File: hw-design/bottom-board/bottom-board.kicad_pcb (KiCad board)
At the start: 2 copper layers, 172 x 140.5 mm, 256 parts, among them J1 JACK_TRS_6PINS, J2 JACK_TRS_6PINS, J3 JACK_TRS_6PINS, J4 JACK_TRS_6PINS, J5 JACK_TRS_6PINS, J6 RJ45_LEDS, J7 Conn_02x50_Odd_Even, J8 Conn_02x50_Odd_Even, K1 IM06TS, K2 IM06TS, P1 USB_B, P2 USB_A, P3 DIN_5, P4 DIN_5, P5 BARREL_JACK, P6 HMI_POWER, P8 HMI_DATA, P9 SERIAL_DEBUG, Q1 2N7002, Q10 2N7002, Q12 2N7002, Q13 2N7002, Q14 BSS84, Q15 BSS84, Q2 2N7002, Q3 J112, Q4 J112, Q5 J112, Q6 J112, Q7 2N7002, Q8 2N7002, Q9 2N7002, SW1 SW_PUSH, U1 MURATA 5V, U10 RT9701, U11 6N137S, U12 ISL83491, U13 AP2120N-3.3, U2 LD1117S50TR_SOT223, U3 CS4245, U4 AT24CS08-STUM, U6 LM4562, U7 LM4562, U8 LM4562, U9 LM4811

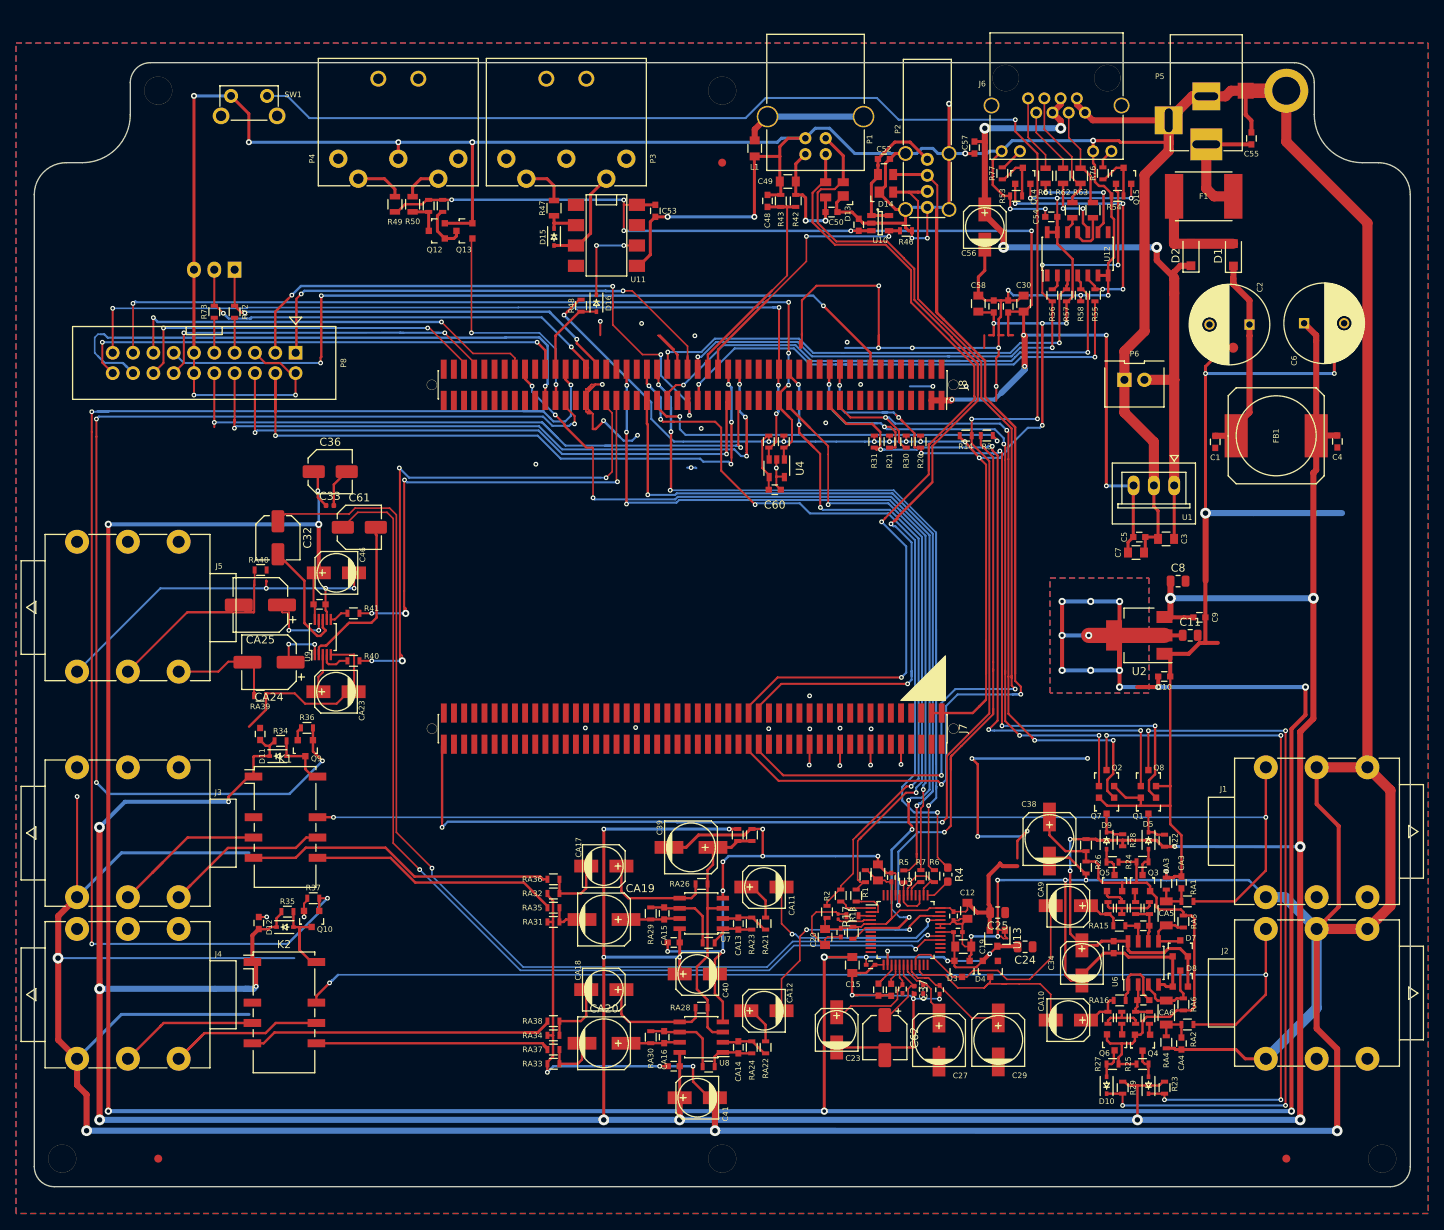
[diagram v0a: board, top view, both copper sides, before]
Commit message: changed a bottomboard to a minimal HMI testing unit
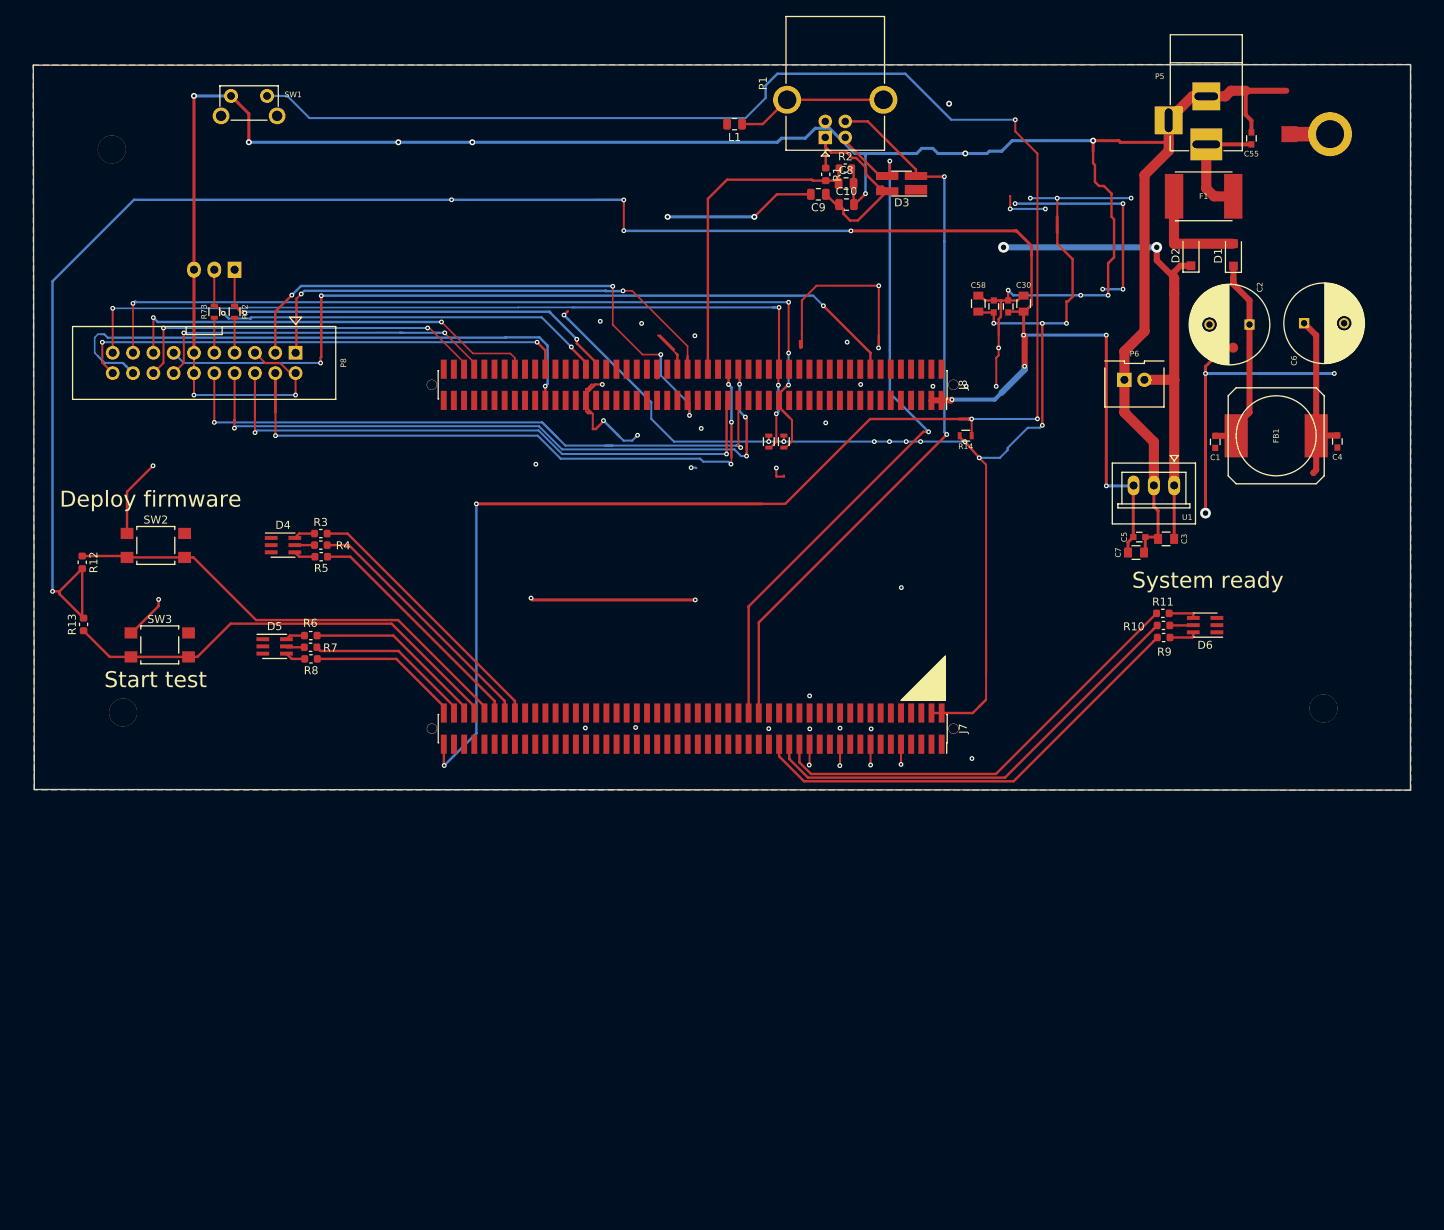
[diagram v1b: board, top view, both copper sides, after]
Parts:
- removed C11, C25: 10uF, Capacitor_SMD:C_0805_2012Metric
- removed C12, C20: 1uF, Capacitors_SMD:C_0805
- removed C13, C14, C16, C17, C21, C22, C26, C28: 100nF, Capacitors_SMD:C_0402
- removed C15, C18, C19, C49: 10uF, Capacitors_SMD:C_0805
- removed C23, C34, C40, C41, C46, C56, CA10, CA11, CA12, CA17, CA18, CA23, CA9: 10uF, Capacitors_SMD:c_elec_5x5.3
- removed C24: 1uF, Capacitor_SMD:C_0805_2012Metric
- removed C27, C29: 47uF, Capacitors_SMD:c_elec_6.3x5.3
- removed C32, C36, C61: 10uF, Capacitor_SMD:C_Elec_5x5.4
- removed C33, C37: 100nF, Capacitor_SMD:C_0402_1005Metric
- removed C35, C42, C43, C44, C45, C47, C48, C50, C51, C52, C53, C54, C57, C60: 100nF, Capacitors_SMD:C_0603
- removed C38, C39: 100uF, Capacitors_SMD:c_elec_6.3x5.3
- removed C62: 10uF, Capacitor_SMD:CP_Elec_5x5.3
- removed CA1, CA2: 2.2nF, Capacitors_SMD:C_0603
- removed CA13, CA14: 33pF, Capacitors_SMD:C_0603
- removed CA15, CA16: 47pF, Capacitors_SMD:C_0603
- removed CA19, CA20: 100uF, Capacitors_SMD:c_elec_6.3x7.7
- removed CA24, CA25: 100uF, Capacitor_SMD:CP_Elec_6.3x7.7
- removed CA3, CA4, CA7, CA8: 100pF, Capacitors_SMD:C_0603
- removed CA5, CA6: 100nF, Capacitors_SMD:C_1206
- removed D10, D11, D12, D15, D16, D9: 1N4148, Diodes_SMD:SOD-323
- removed D13, D14: PRTR5V0U2X, Housings_SOT-23_SOT-143_TSOT-6:SOT-143
- removed D7, D8: BAS70-04, Housings_SOT-23_SOT-143_TSOT-6:SOT-23
- removed FID1, FID2, FID3: FIDUCIAL, footprints:fiducial_in-circuit
- removed H3, H4: HOLE, footprints:Hole_3.5mm
- removed J1, J2, J3, J4, J5: JACK_TRS_6PINS, Connect:NMJ6HCD2
- removed J6: RJ45_LEDS, Connect:RJHSE538X
- removed K1, K2: IM06TS, footprints:Relay_DPDT_Omron_G6S-2F-good_pinout
- removed P2: USB_A, Connect:USB_A_Vertical
- removed P3, P4: DIN_5, Connect:SDS-50J
- removed Q1, Q10, Q12, Q13, Q2, Q7, Q8, Q9: 2N7002, Housings_SOT-23_SOT-143_TSOT-6:SOT-23
- removed Q14, Q15: BSS84, Housings_SOT-23_SOT-143_TSOT-6:SOT-23
- removed Q3, Q4, Q5, Q6: J112, Housings_SOT-23_SOT-143_TSOT-6:SOT-23
- removed R17: 10k, Resistor_SMD:R_0201_0603Metric
- removed R20, R21, R30, R31, R36, R37, R43, R46, R48, R51, R52, R53, R54, R57, R58, RA21, RA22, RA25, RA26, RA27, RA28, RA29, RA30: 10k, Resistors_SMD:R_0603
- removed R22, R23, R28, R29, R34, R35: 100k, Resistors_SMD:R_0603
- removed R24, R25, R26, R27, RA3, RA4, RA5, RA6: 1M, Resistors_SMD:R_0603
- removed R40, R41: 22R, Resistors_SMD:R_0603
- removed R42: 5k6, Resistors_SMD:R_0603
- removed R47, R49, R50: 220R, Resistors_SMD:R_0805
- removed R55, R56, RA15, RA16: 100R, Resistors_SMD:R_0603
- removed R59, R60, R61, R62: 56R, Resistors_SMD:R_0805
- removed R63: 100R, Resistors_SMD:R_0805
- removed R76, R77: 330R, Resistors_SMD:R_0603
- removed RA1, RA2: 47R, Resistors_SMD:R_0603
- removed RA10, RA9: 21k, Resistors_SMD:R_0603
- removed RA11, RA12, RA7, RA8: 1k5, Resistors_SMD:R_0603
- removed RA13, RA14: 4k99, Resistors_SMD:R_0603
- removed RA17, RA18, RA19, RA20: 1k2, Resistors_SMD:R_0603
- removed RA23, RA24: 15k, Resistors_SMD:R_0603
- removed RA31, RA33: 22k, Resistors_SMD:R_0603
- removed RA32, RA34, RA36, RA38: 33R, Resistors_SMD:R_0603
- removed RA35, RA37: 66R, Resistors_SMD:R_0603
- removed RA39, RA40: 75k, Resistors_SMD:R_0603
- removed U10: RT9701, Housings_SOT-23_SOT-143_TSOT-6:SOT-23-5
- removed U11: 6N137S, SMD_Packages:DIP-8_SMD
- removed U12: ISL83491, Housings_SOIC:SOIC-14_3.9x8.7mm_Pitch1.27mm
- removed U13: AP2120N-3.3, Package_TO_SOT_SMD:SOT-23
- removed U2: LD1117S50TR_SOT223, Package_TO_SOT_SMD:SOT-223-3_TabPin2
- removed U3: CS4245, Package_QFP:LQFP-48_7x7mm_P0.5mm
- removed U4: AT24CS08-STUM, Package_TO_SOT_SMD:SOT-23-5
- removed U6, U7, U8: LM4562, Housings_SOIC:SOIC-8_3.9x4.9mm_Pitch1.27mm
- removed U9: LM4811, Housings_SSOP:MSOP-10_3x3mm_Pitch0.5mm
- added R11: 100, Resistor_SMD:R_0603_1608Metric, F.Cu at (201.1, 88.4)
- added R8: 100, Resistor_SMD:R_0603_1608Metric, F.Cu at (94.7, 94.1)
- added SW2: SW_PUSH, Button_Switch_SMD:SW_SPST_TL3305A, F.Cu at (75.3, 79.9)
- added SW3: SW_PUSH, Button_Switch_SMD:SW_SPST_TL3305A, F.Cu at (75.8, 92.3)
- C10: footprint Capacitors_SMD:C_0603 -> Capacitor_SMD:C_0805_2012Metric
- C8: value 10uF -> 100nF
- C9: value 100nF -> 10u; footprint Capacitors_SMD:C_0603 -> Capacitor_SMD:C_0805_2012Metric
- D3: value BAS70-04 -> PRTR5V0U2X; footprint Housings_SOT-23_SOT-143_TSOT-6:SOT-23 -> Package_TO_SOT_SMD:SOT-143_Handsoldering
- D4: value BAS70-04 -> LED_RGB; footprint Housings_SOT-23_SOT-143_TSOT-6:SOT-23 -> LED_SMD:LED_Avago_PLCC6_3x2.8mm
- D5, D6: value 1N4148 -> LED_RGB; footprint Diodes_SMD:SOD-323 -> LED_SMD:LED_Avago_PLCC6_3x2.8mm
- G***: moved to F.Cu
- L1: footprint Capacitors_SMD:C_0805 -> Capacitor_SMD:C_0805_2012Metric
- P1: value USB_B -> USB_B-RESCUE-bottom-board; footprint Connect:USB_B -> Connector_USB:USB_B_OST_USB-B1HSxx_Horizontal
- R1: value 10k -> 5k6; footprint Resistors_SMD:R_0603 -> Resistor_SMD:R_0603_1608Metric
- R10, R3, R5, R6, R7, R9: value 22R -> 100; footprint Resistors_SMD:R_0603 -> Resistor_SMD:R_0603_1608Metric
- R12, R13, R2: value 10k -> 10K; footprint Resistors_SMD:R_0603 -> Resistor_SMD:R_0603_1608Metric
- R4: value 22R -> 100; footprint Resistor_SMD:R_0603_1608Metric_Pad1.05x0.95mm_HandSolder -> Resistor_SMD:R_0603_1608Metric
- moved D5 111.9 mm to (90.1, 92.5), turned to 0 degrees
- moved H2 107.8 mm to (221.2, 100.3)
- moved R12 105.9 mm to (66.1, 82.0), turned to 270 degrees
- moved R13 103.6 mm to (66.2, 89.8), turned to 90 degrees
- moved D4 103.1 mm to (91.2, 79.9), turned to 0 degrees
- moved D3 98.5 mm to (168.5, 34.7)
- moved H1 93.4 mm to (71.2, 100.8)
- moved R2 93.0 mm to (161.5, 32.7), turned to 0 degrees
- moved R4 88.5 mm to (95.9, 79.9), turned to 180 degrees
- moved R1 87.9 mm to (159.0, 33.5), turned to 270 degrees
- moved R3 84.1 mm to (95.9, 78.4), turned to 180 degrees
- moved R6 83.5 mm to (94.6, 91.2), turned to 180 degrees
- moved R5 83.1 mm to (95.9, 81.3), turned to 180 degrees
- moved R7 81.5 mm to (94.6, 92.6), turned to 180 degrees
- moved C9 71.2 mm to (158.1, 36.0), turned to 180 degrees
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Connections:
- C10 pad 1: +5VA -> Net-(C10-Pad1)
- C8 pad 1: +12VA -> USB_DEV_DET
- C9 pad 1: +12VA -> Net-(C10-Pad1)
- D3 pad 2: +5VA -> USB_DEV_DP
- D3 pad 3: CODEC_ADC_A -> USB_DEV_DM
- D4 pad 2: +5VA -> GNDA
- D4 pad 3: CODEC_ADC_B -> GNDA
- D5 pad 1: Net-(D5-Pad1) -> GNDA
- D5 pad 2: Net-(D5-Pad2) -> GNDA
- D6 pad 1: Net-(D6-Pad1) -> GNDA
- D6 pad 2: Net-(D6-Pad2) -> GNDA
- J7 pad 100: Net-(J7-Pad100) -> LED2_R
- J7 pad 11: Net-(J7-Pad11) -> (no net)
- J7 pad 12: Net-(J7-Pad12) -> (no net)
- J7 pad 13: Net-(J7-Pad13) -> (no net)
- J7 pad 14: Net-(J7-Pad14) -> (no net)
- J7 pad 17: Net-(J7-Pad17) -> (no net)
- J7 pad 18: Net-(J7-Pad18) -> (no net)
- J7 pad 19: Net-(J7-Pad19) -> (no net)
- J7 pad 20: Net-(J7-Pad20) -> (no net)
- J7 pad 23: Net-(J7-Pad23) -> (no net)
- J7 pad 24: Net-(J7-Pad24) -> (no net)
- J7 pad 25: Net-(J7-Pad25) -> (no net)
- J7 pad 26: Net-(J7-Pad26) -> (no net)
- J7 pad 29: Net-(J7-Pad29) -> LED3_R
- J7 pad 30: Net-(J7-Pad30) -> (no net)
- J7 pad 31: Net-(J7-Pad31) -> LED3_G
- J7 pad 32: Net-(J7-Pad32) -> (no net)
- J7 pad 33: Net-(J7-Pad33) -> LED3_B
- J7 pad 34: Net-(J7-Pad34) -> (no net)
- J7 pad 37: USB_HOST_DP -> (no net)
- J7 pad 39: USB_HOST_DM -> (no net)
- J7 pad 42: Net-(J7-Pad42) -> (no net)
- J7 pad 43: Net-(J7-Pad43) -> (no net)
- J7 pad 44: Net-(J7-Pad44) -> (no net)
- J7 pad 45: Net-(J7-Pad45) -> (no net)
- J7 pad 46: Net-(J7-Pad46) -> (no net)
- J7 pad 48: Net-(J7-Pad48) -> (no net)
- J7 pad 49: Net-(J7-Pad49) -> (no net)
- J7 pad 5: Net-(J7-Pad5) -> (no net)
- J7 pad 50: Net-(J7-Pad50) -> (no net)
- J7 pad 51: Net-(J7-Pad51) -> (no net)
- J7 pad 52: Net-(J7-Pad52) -> (no net)
- J7 pad 53: Net-(J7-Pad53) -> (no net)
- J7 pad 54: Net-(J7-Pad54) -> (no net)
- J7 pad 55: Net-(J7-Pad55) -> (no net)
- J7 pad 56: Net-(J7-Pad56) -> (no net)
- J7 pad 57: Net-(J7-Pad57) -> (no net)
- J7 pad 58: Net-(J7-Pad58) -> (no net)
- J7 pad 59: Net-(J7-Pad59) -> (no net)
- J7 pad 6: Net-(J7-Pad6) -> (no net)
- J7 pad 60: Net-(J7-Pad60) -> (no net)
- J7 pad 63: Net-(J7-Pad63) -> (no net)
- J7 pad 64: Net-(J7-Pad64) -> (no net)
- J7 pad 65: Net-(J7-Pad65) -> (no net)
- J7 pad 66: Net-(J7-Pad66) -> (no net)
- J7 pad 67: Net-(J7-Pad67) -> (no net)
- J7 pad 68: Net-(J7-Pad68) -> (no net)
- J7 pad 69: Net-(J7-Pad69) -> (no net)
- J7 pad 7: Net-(J7-Pad7) -> (no net)
- J7 pad 70: Net-(J7-Pad70) -> (no net)
- J7 pad 71: Net-(J7-Pad71) -> (no net)
- J7 pad 73: Net-(J7-Pad73) -> (no net)
- J7 pad 74: Net-(J7-Pad74) -> (no net)
- J7 pad 75: Net-(J7-Pad75) -> (no net)
- J7 pad 76: Net-(J7-Pad76) -> (no net)
- J7 pad 77: Net-(J7-Pad77) -> (no net)
- J7 pad 78: Net-(J7-Pad78) -> (no net)
- J7 pad 79: Net-(J7-Pad79) -> (no net)
- J7 pad 8: Net-(J7-Pad8) -> (no net)
- J7 pad 80: Net-(J7-Pad80) -> (no net)
- J7 pad 81: Net-(J7-Pad81) -> (no net)
- J7 pad 82: Net-(J7-Pad82) -> (no net)
- J7 pad 83: Net-(J7-Pad83) -> (no net)
- J7 pad 84: Net-(J7-Pad84) -> (no net)
- J7 pad 85: Net-(J7-Pad85) -> (no net)
- J7 pad 86: Net-(J7-Pad86) -> LED1_B
- J7 pad 87: Net-(J7-Pad87) -> (no net)
- J7 pad 88: Net-(J7-Pad88) -> LED1_G
- J7 pad 89: Net-(J7-Pad89) -> (no net)
- J7 pad 90: Net-(J7-Pad90) -> LED1_R
- J7 pad 91: Net-(J7-Pad91) -> (no net)
- J7 pad 92: Net-(J7-Pad92) -> Button1
- J7 pad 93: Net-(J7-Pad93) -> (no net)
- J7 pad 94: Net-(J7-Pad94) -> Button2
- J7 pad 95: Net-(J7-Pad95) -> (no net)
- J7 pad 96: Net-(J7-Pad96) -> LED2_B
- J7 pad 97: Net-(J7-Pad97) -> (no net)
- J7 pad 98: Net-(J7-Pad98) -> LED2_G
- J8 pad 100: Net-(J8-Pad100) -> (no net)
- J8 pad 11: Net-(J8-Pad11) -> (no net)
- J8 pad 12: Net-(J8-Pad12) -> (no net)
- J8 pad 13: Net-(J8-Pad13) -> (no net)
- J8 pad 14: Net-(J8-Pad14) -> (no net)
- J8 pad 15: Net-(J8-Pad15) -> (no net)
- J8 pad 17: Net-(J8-Pad17) -> (no net)
- J8 pad 19: Net-(J8-Pad19) -> (no net)
- J8 pad 20: Net-(J8-Pad20) -> (no net)
- J8 pad 21: LEFT_GAIN_CTRL2 -> (no net)
- J8 pad 22: LEFT_GAIN_CTRL1 -> (no net)
- J8 pad 23: RIGHT_GAIN_CTRL2 -> (no net)
- J8 pad 24: RIGHT_GAIN_CTRL1 -> (no net)
- J8 pad 25: Net-(J8-Pad25) -> (no net)
- J8 pad 26: Net-(J8-Pad26) -> (no net)
- J8 pad 27: Net-(J8-Pad27) -> (no net)
- J8 pad 28: Net-(J8-Pad28) -> (no net)
- J8 pad 29: Net-(J8-Pad29) -> (no net)
- J8 pad 30: Net-(J8-Pad30) -> (no net)
- J8 pad 31: CODEC_I2C_SCL -> (no net)
- J8 pad 32: CODEC_I2C_SDA -> (no net)
- J8 pad 35: Net-(J8-Pad35) -> (no net)
- J8 pad 36: Net-(J8-Pad36) -> (no net)
- J8 pad 37: Net-(J8-Pad37) -> (no net)
- J8 pad 38: Net-(J8-Pad38) -> (no net)
- J8 pad 39: Net-(J8-Pad39) -> (no net)
- J8 pad 40: Net-(J8-Pad40) -> (no net)
- J8 pad 45: Net-(J8-Pad45) -> (no net)
- J8 pad 46: USB_HOST_DRV -> (no net)
- J8 pad 47: Net-(J8-Pad47) -> (no net)
- J8 pad 49: CHAIN_UART_TX -> (no net)
- J8 pad 5: Net-(J8-Pad5) -> (no net)
- J8 pad 50: CHAIN_UART_RX -> (no net)
- J8 pad 53: Net-(J8-Pad53) -> (no net)
- J8 pad 55: CHAIN_UART_DE -> (no net)
- J8 pad 56: CHAIN_UART_RE -> (no net)
- J8 pad 57: CODEC_I2S_MCLK -> (no net)
- J8 pad 58: CODEC_I2S_BCLK -> (no net)
- J8 pad 59: CODEC_I2S_LRCK -> (no net)
- J8 pad 6: Net-(J8-Pad6) -> (no net)
- J8 pad 60: CODEC_I2S_SDIN -> (no net)
- J8 pad 61: Net-(J8-Pad61) -> (no net)
- J8 pad 62: Net-(J8-Pad62) -> (no net)
- J8 pad 63: Net-(J8-Pad63) -> (no net)
- J8 pad 64: CODEC_I2S_SDOUT -> (no net)
- J8 pad 65: HP_UP/DN -> (no net)
- J8 pad 66: Net-(J8-Pad66) -> (no net)
- J8 pad 67: HP_CLOCK -> (no net)
- J8 pad 68: Net-(J8-Pad68) -> (no net)
- J8 pad 69: Net-(J8-Pad69) -> (no net)
- J8 pad 7: Net-(J8-Pad7) -> (no net)
- J8 pad 73: Net-(J8-Pad73) -> (no net)
- J8 pad 74: Net-(J8-Pad74) -> (no net)
- J8 pad 75: LEFT_TRUE_BYPASS -> (no net)
- J8 pad 76: RIGHT_TRUE_BYPASS -> (no net)
- J8 pad 77: MIDI_UART_TX -> (no net)
- J8 pad 78: MIDI_UART_RX -> (no net)
- J8 pad 8: Net-(J8-Pad8) -> (no net)
- J8 pad 81: Net-(J8-Pad81) -> (no net)
- J8 pad 82: Net-(J8-Pad82) -> (no net)
- J8 pad 83: Net-(J8-Pad83) -> (no net)
- J8 pad 84: CODEC_~RESET -> (no net)
- J8 pad 85: Net-(J8-Pad85) -> (no net)
- J8 pad 87: Net-(J8-Pad87) -> (no net)
- J8 pad 88: Net-(J8-Pad88) -> (no net)
- J8 pad 89: Net-(J8-Pad89) -> (no net)
- J8 pad 9: Net-(J8-Pad9) -> (no net)
- J8 pad 90: Net-(J8-Pad90) -> (no net)
- J8 pad 91: Net-(J8-Pad91) -> (no net)
- J8 pad 92: Net-(J8-Pad92) -> (no net)
- J8 pad 93: Net-(J8-Pad93) -> (no net)
- J8 pad 95: Net-(J8-Pad95) -> (no net)
- J8 pad 97: Net-(J8-Pad97) -> (no net)
- J8 pad 98: Net-(J8-Pad98) -> (no net)
- J8 pad 99: Net-(J8-Pad99) -> (no net)
- P1 pad 1: Net-(C49-Pad1) -> Net-(C10-Pad1)
- R1 pad 1: CODEC_I2C_SCL -> Net-(C10-Pad1)
- R1 pad 2: +3.3VA -> USB_DEV_DET
- R10 pad 1: Net-(R10-Pad1) -> LED3_G
- R10 pad 2: CODEC_I2C_SCL -> Net-(D6-Pad5)
- R12 pad 1: GNDA -> Button1
- R12 pad 2: Net-(R12-Pad2) -> +5V
- R13 pad 1: +3.3VA -> Button2
- R13 pad 2: CODEC_~RESET -> +5V
- R2 pad 1: CODEC_I2C_SDA -> USB_DEV_DET
- R2 pad 2: +3.3VA -> GNDA
- R3 pad 1: Net-(R3-Pad1) -> LED1_B
- R3 pad 2: CODEC_I2S_MCLK -> Net-(D4-Pad6)
- R4 pad 1: CODEC_I2S_SDIN -> LED1_G
- R4 pad 2: Net-(R4-Pad2) -> Net-(D4-Pad5)
- R5 pad 1: Net-(R5-Pad1) -> LED1_R
- R5 pad 2: CODEC_I2S_LRCK -> Net-(D4-Pad4)
- R6 pad 1: Net-(R6-Pad1) -> LED2_B
- R6 pad 2: CODEC_I2S_BCLK -> Net-(D5-Pad6)
- R7 pad 1: Net-(R7-Pad1) -> LED2_G
- R7 pad 2: CODEC_I2S_SDOUT -> Net-(D5-Pad5)
- R9 pad 1: Net-(R9-Pad1) -> LED3_B
- R9 pad 2: CODEC_I2C_SDA -> Net-(D6-Pad6)
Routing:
- net GNDA: track 1596.5 -> 506.8 mm, vias 86 -> 56
- net +12VA: track 531.6 -> 22.2 mm, vias 19 -> 0
- net +5VA: track 471.3 -> 0.00 mm, vias 22 -> 0
- net RIGHT_TRUE_BYPASS: track 174.6 -> 0.00 mm, vias 4 -> 0
- net LEFT_TRUE_BYPASS: track 145.5 -> 0.00 mm, vias 4 -> 0
- net LEFT_AUDIO_INPUT: track 142.1 -> 0.00 mm, vias 2 -> 0
- net RIGHT_AUDIO_INPUT: track 139.4 -> 0.00 mm, vias 2 -> 0
- net USB_HOST_DM: track 136.1 -> 0.00 mm, vias 2 -> 0
- net CODEC_AUX_B: track 132.8 -> 0.00 mm, vias 2 -> 0
- net CODEC_I2S_BCLK: track 127.5 -> 0.00 mm, vias 4 -> 0
- net CODEC_~RESET: track 125.5 -> 0.00 mm, vias 6 -> 0
- net CODEC_AUX_A: track 124.9 -> 0.00 mm, vias 2 -> 0
- net USB_HOST_DP: track 116.2 -> 0.00 mm, vias 2 -> 0
- net CODEC_I2S_SDOUT: track 98.4 -> 0.00 mm, vias 4 -> 0
- net CODEC_I2S_SDIN: track 96.9 -> 0.00 mm, vias 4 -> 0
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- removed copper zone on B.Cu, net +5VA
- removed copper zone on F.Cu, net +5VA
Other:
- board size 172 x 140.5 mm -> 172.2 x 90.7 mm
- board text added: "Deploy firmware"
- board text added: "MOD Devices GmbH http://moddevices.com MOD-HMI verification board Rev 2019.06.10"
- board text added: "Start test"
- board text added: "System ready"
- board text removed: "MOD Devices GmbH http://moddevices.com [DU-ELE-001] MOD Duo - Bottom Board Rev.: 2019.04.15"
